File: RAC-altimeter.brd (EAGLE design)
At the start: 160 x 100 mm, 33 parts, among them J1 282834-2, J2 CORTEX_DEBUG_SMD, J3 MICRO-SD, J4 JUMPER-SMT_2_NO_SILK, U1 MAX32660GTP+, U2 BMI088, U3 BMP388, U4 RN4871-I_RM130, U5 MCP1640T-I_CHY, Y1 32.768kHz

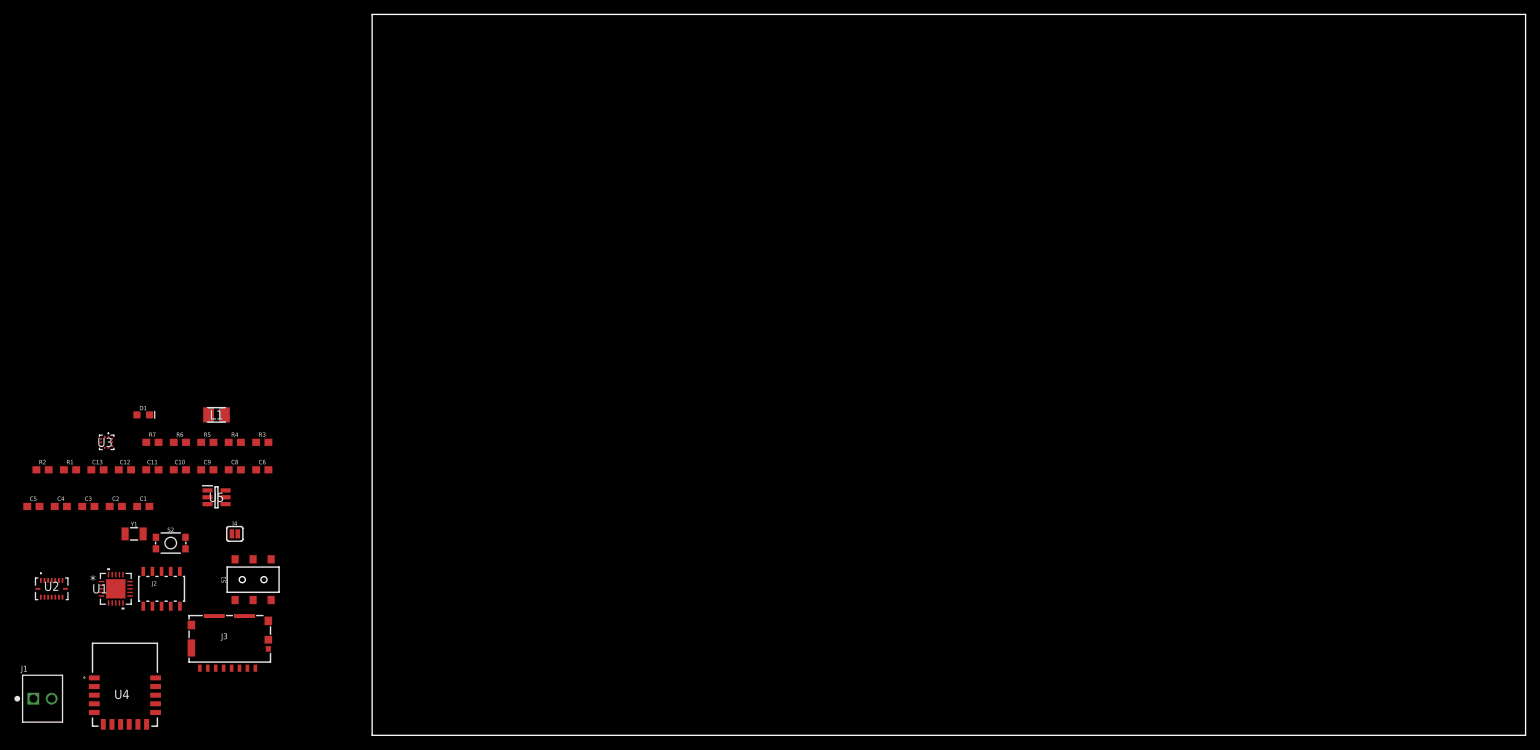
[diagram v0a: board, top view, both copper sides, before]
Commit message: Fixed net connections and routed IC groups
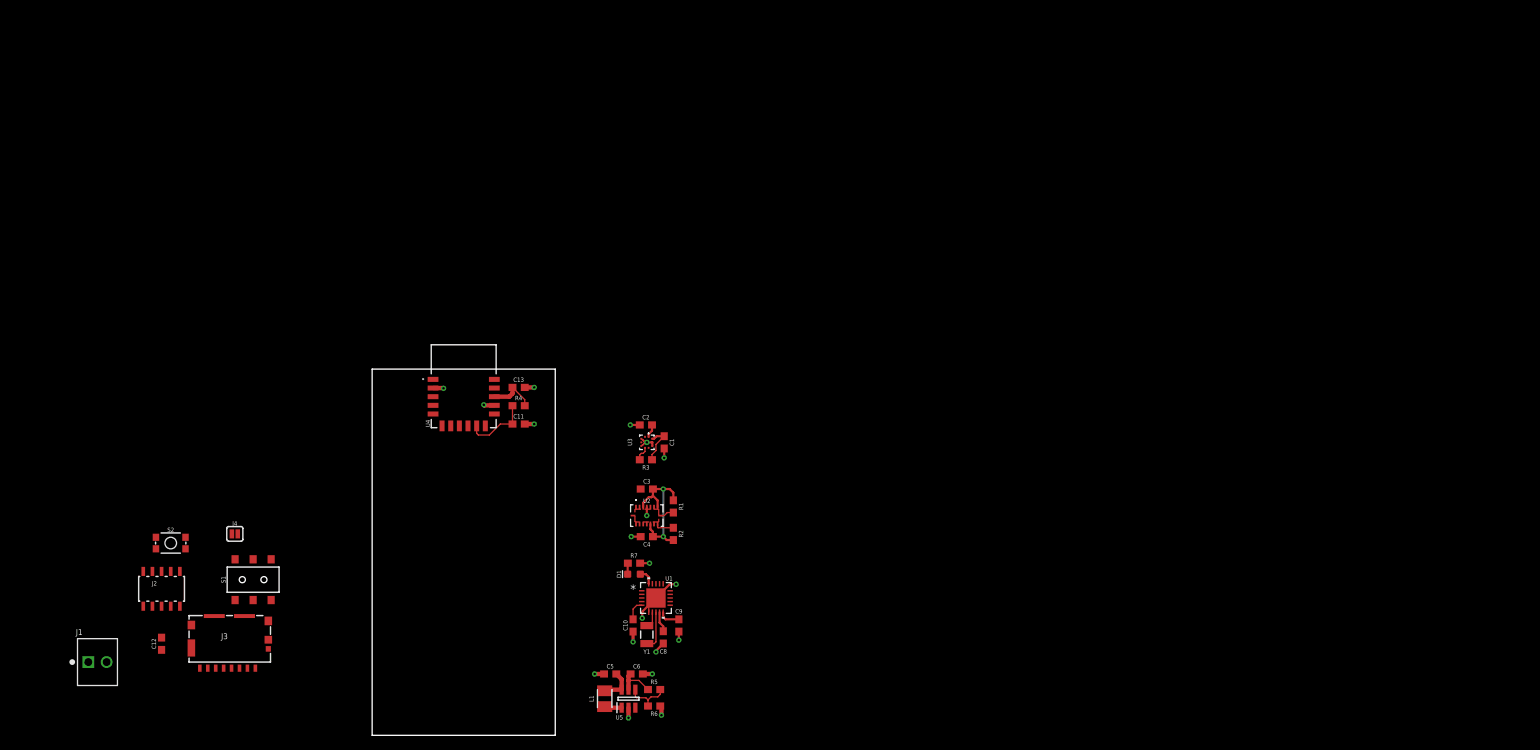
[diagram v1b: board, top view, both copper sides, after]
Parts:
- moved R2 88.0 mm to (41.8, 27.9), turned to 270 degrees
- moved R1 83.8 mm to (41.8, 31.8), turned to 90 degrees
- moved C5 83.3 mm to (33.0, 8.51), turned to 180 degrees
- moved U2 83.2 mm to (38.1, 30.5)
- moved C4 81.4 mm to (38.1, 27.6)
- moved C3 77.5 mm to (38.1, 34.2), turned to 180 degrees
- moved R6 75.3 mm to (39.1, 4.06), turned to 180 degrees
- moved U1 74.9 mm to (39.4, 19.1)
- moved U3 74.9 mm to (38.1, 40.6)
- moved C2 74.4 mm to (38.0, 43.1), turned to 180 degrees
- moved C1 72.8 mm to (40.5, 40.6), turned to 270 degrees
- moved Y1 72.5 mm to (38.1, 14.0), turned to 90 degrees
- moved D1 71.6 mm to (36.3, 22.4), turned to 180 degrees
- moved R5 70.8 mm to (39.1, 6.35), turned to 180 degrees
- moved C9 68.9 mm to (42.5, 15.2), turned to 270 degrees
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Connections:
- net N$10 renamed 32KOUT
- net N$11 renamed VCORE
- net N$2 renamed SW
- net N$3 renamed VFB
- net N$9 renamed 32KIN
- removed net N$4: C1.2, U3.10
- removed net N$5: C2.1, U3.1
- removed net N$6: C2.2, U3.3
- net GND: now also C1.2, C2.2, U3.3; no longer C1.1
- net IO_LED: now also U1.20; no longer U1.19
- net VCC: now also C1.1, C2.1, U3.1, U3.10
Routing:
- net VCC: track 0.00 -> 43.6 mm, vias 0 -> 2
- net GND: track 0.00 -> 34.0 mm, vias 0 -> 19
- net !RSTN: track 0.00 -> 12.1 mm
- net VFB: track 0.00 -> 6.43 mm
- net 32KIN: track 0.00 -> 5.49 mm
- net V_BATT: track 0.00 -> 4.90 mm
- net VCORE: track 0.00 -> 2.99 mm
- net I2C0_SDA: track 0.00 -> 2.67 mm
- net 32KOUT: track 0.00 -> 2.47 mm
- net SW: track 0.00 -> 2.41 mm
- net IO_LED: track 0.00 -> 2.27 mm
- net BMP_CS: track 0.00 -> 2.10 mm
- net I2C0_SCL: track 0.00 -> 1.94 mm
- net LED_CATH: track 0.00 -> 1.54 mm
- added copper zone on layer 1, net GND
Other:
- board size 160 x 100 mm -> 25.4 x 50.8 mm

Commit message: Added PCB mounting holes
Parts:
- added H1, H2, H3, H4: MOUNT-HOLE2.8, holes:2,8
- moved R4 6.56 mm to (15.6, 41.1)
- moved C13 6.47 mm to (18.5, 42.0), turned to 270 degrees
- moved C11 5.89 mm to (15.6, 39.6)
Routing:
- net !RSTN: track 12.1 -> 6.27 mm
- net VCC: track 43.6 -> 46.6 mm, vias 2 -> 4
- net GND: track 34.0 -> 32.0 mm, vias 19 -> 16

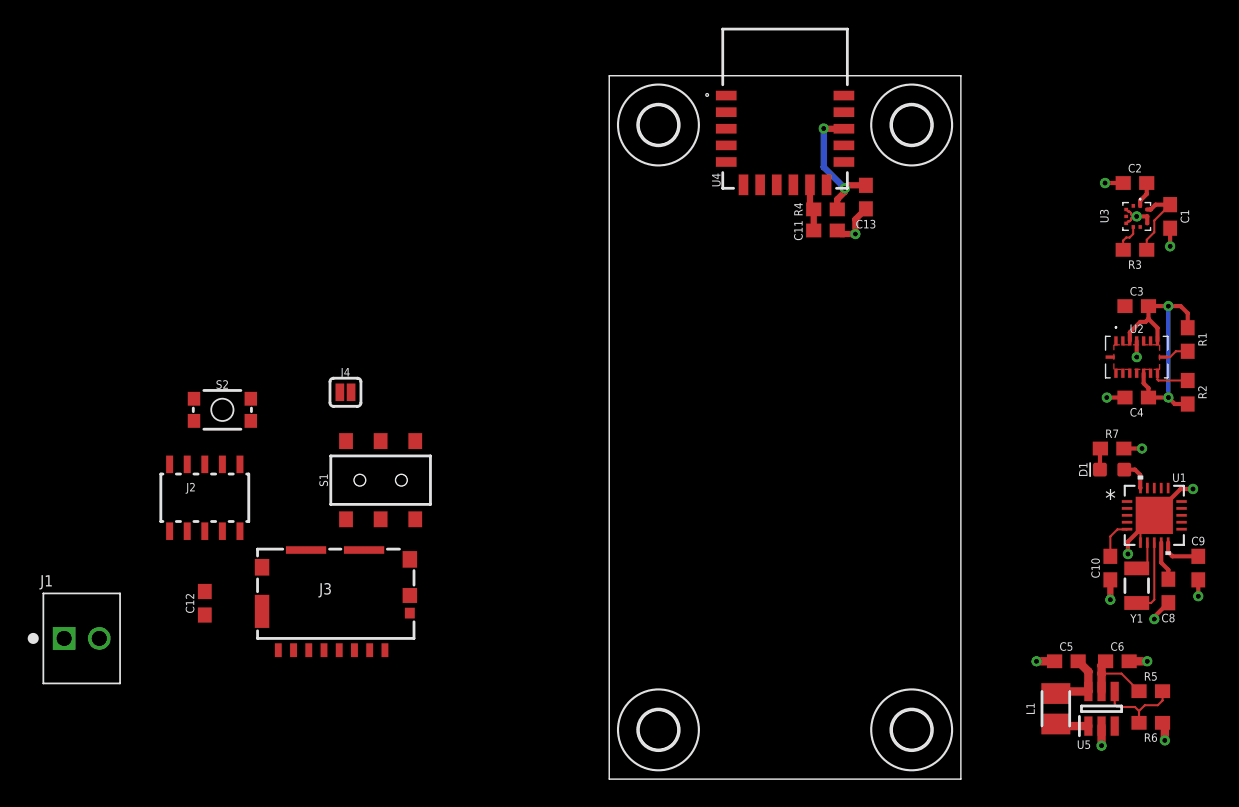
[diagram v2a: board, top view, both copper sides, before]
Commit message: Closed loose nets and finished routing
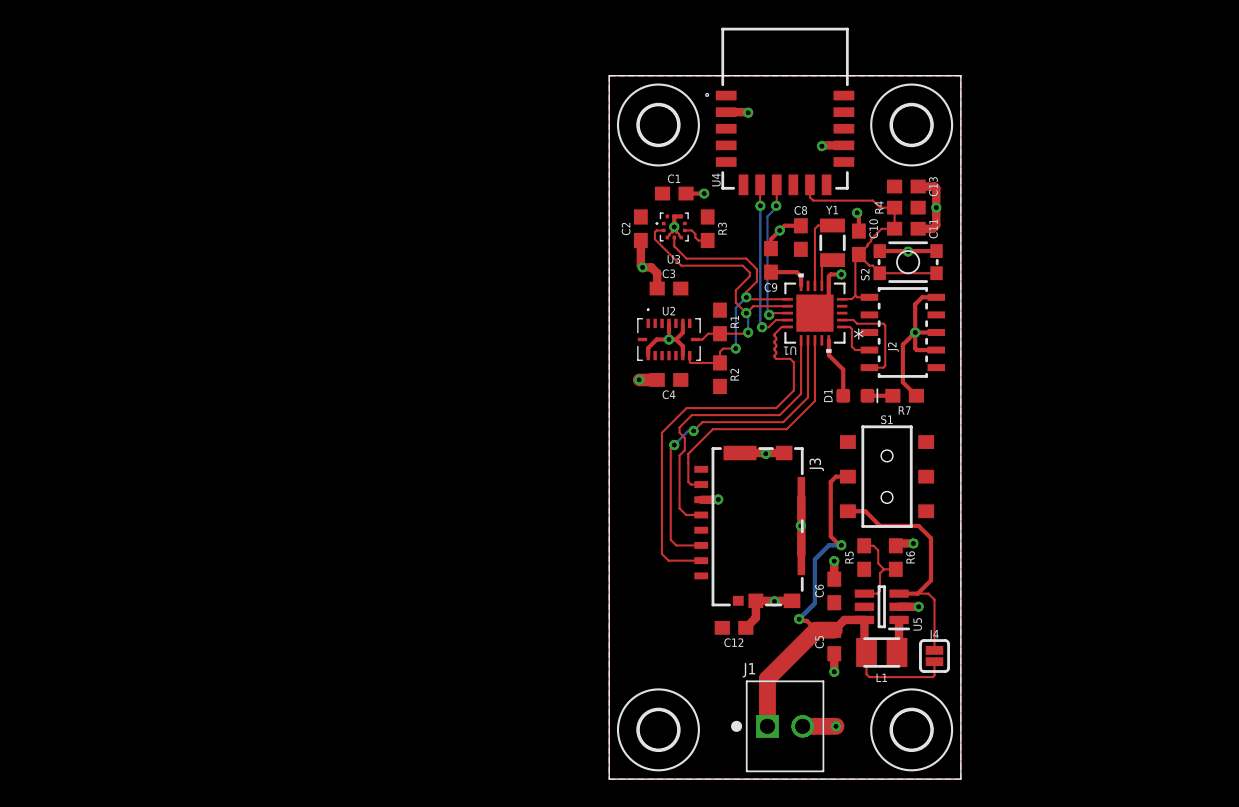
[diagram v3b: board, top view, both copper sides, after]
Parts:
- moved J2 51.8 mm to (21.2, 32.3), turned to 90 degrees
- moved J1 51.2 mm to (12.7, 3.81)
- moved S2 50.7 mm to (21.6, 37.3)
- moved J4 46.6 mm to (23.5, 8.89), turned to 90 degrees
- moved C12 38.3 mm to (9.02, 10.9), turned to 0 degrees
- moved C9 38.0 mm to (11.7, 37.5), turned to 90 degrees
- moved C8 36.8 mm to (13.8, 39.1), turned to 90 degrees
- moved S1 36.6 mm to (20.1, 21.8), turned to 90 degrees
- moved C1 35.9 mm to (4.70, 42.3), turned to 0 degrees
- moved C2 35.8 mm to (2.29, 39.8), turned to 270 degrees
- moved J3 35.6 mm to (7.49, 23.9), turned to 270 degrees
- moved C3 33.8 mm to (4.32, 35.4)
- moved C4 33.8 mm to (4.32, 28.8)
- moved R1 33.8 mm to (8.00, 33.0)
- moved R2 33.8 mm to (8.00, 29.2)
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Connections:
- net BOOST_EN: now also S1.1; no longer S1.3
- net GND: now also J3.GND1, J3.GND2, J3.GND3, J3.GND4, J3.GND5, J3.GND6
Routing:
- net VCC: track 46.6 -> 0.00 mm, vias 4 -> 0
- net GND: track 32.0 -> 73.0 mm, vias 16 -> 22
- net V_BATT: track 4.90 -> 37.3 mm, vias 0 -> 2
- net CS_SD: track 0.00 -> 29.3 mm
- net SPI0_MOSI: track 0.00 -> 24.5 mm, vias 0 -> 2
- net SPI0_SCK: track 0.00 -> 21.6 mm
- net I2C0_SCL: track 1.94 -> 21.4 mm, vias 0 -> 2
- net I2C0_SDA: track 2.67 -> 21.4 mm, vias 0 -> 2
- net SPI0_MISO: track 0.00 -> 18.1 mm
- net BOOST_EN: track 0.00 -> 17.6 mm
- net !RSTN: track 6.27 -> 23.7 mm
- net UART1_TX: track 0.00 -> 12.4 mm, vias 0 -> 2
- net UART1_RX: track 0.00 -> 11.1 mm, vias 0 -> 2
- net SWDIO: track 0.00 -> 7.39 mm
- net SWDCLK: track 0.00 -> 3.40 mm
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- added copper zone on layer 16, net GND
- added copper zone on layer 1, net VCC
- removed copper zone on layer 1, net GND
